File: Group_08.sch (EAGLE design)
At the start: 29 parts, among them J1 POWER_JACKPTH_LOCK, U1 +12v, U3 TCA9546ATSSOP, U4 TMUX1208

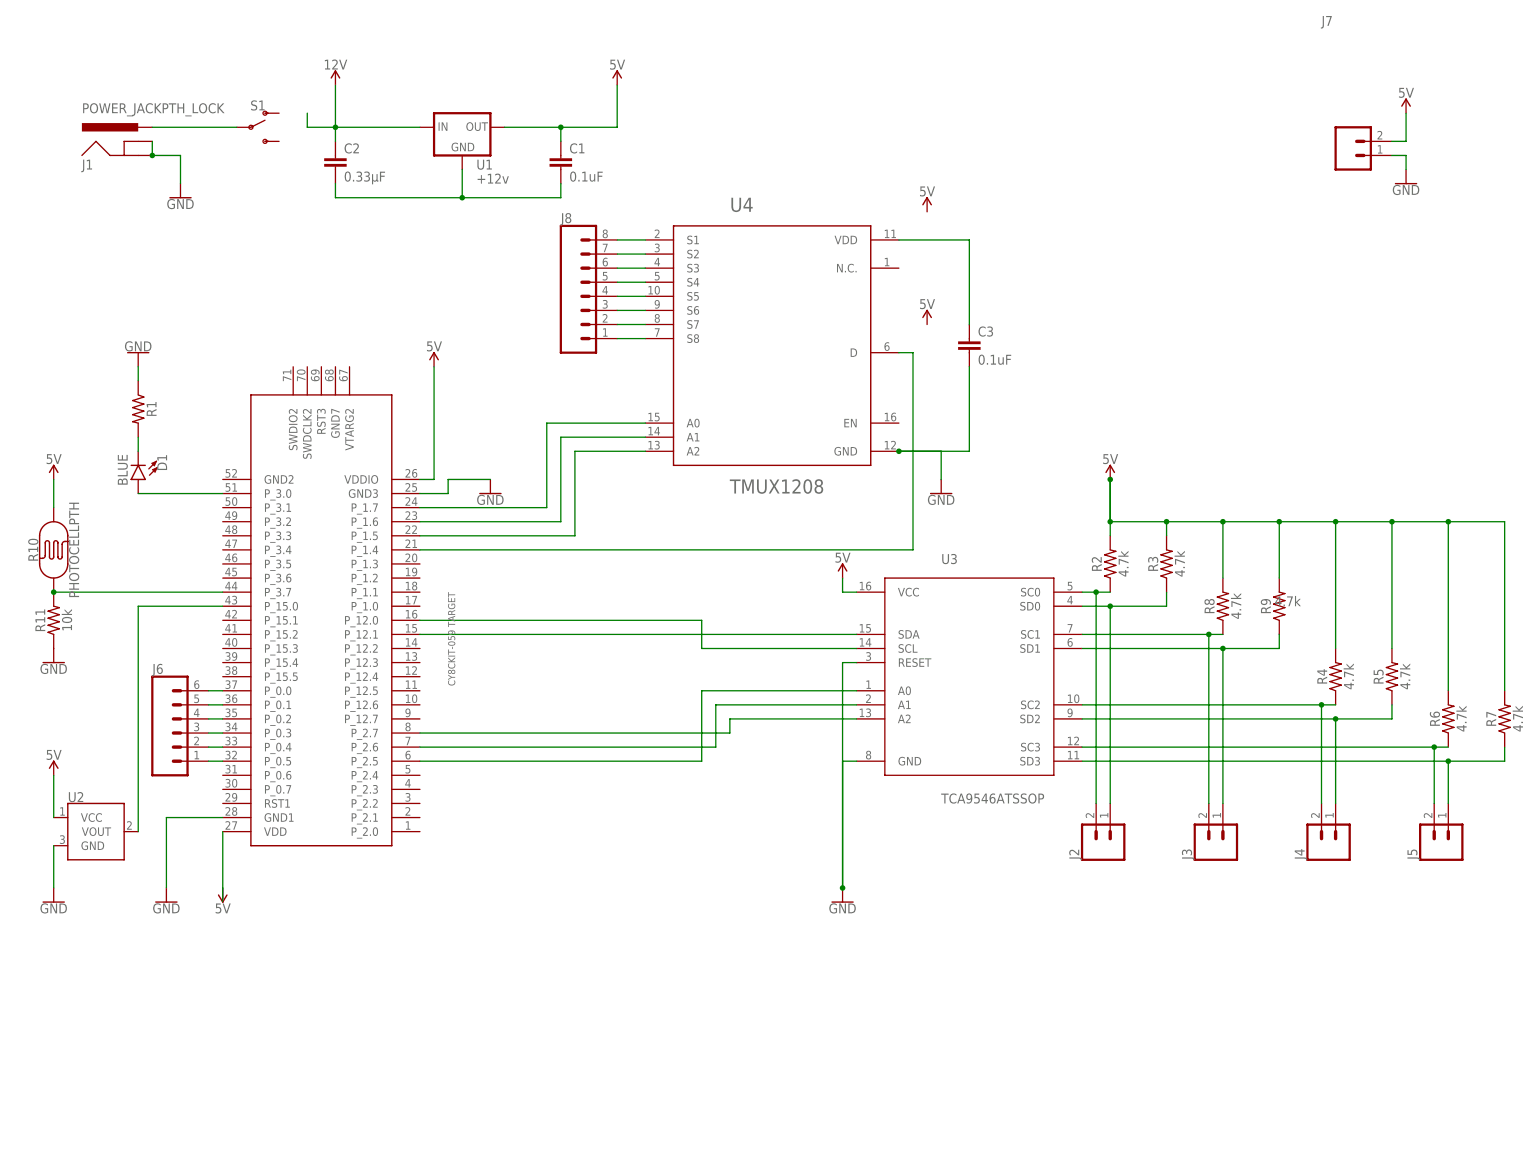
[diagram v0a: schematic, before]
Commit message: Fixed wiring and did small aesthetic adjustments to library symbols
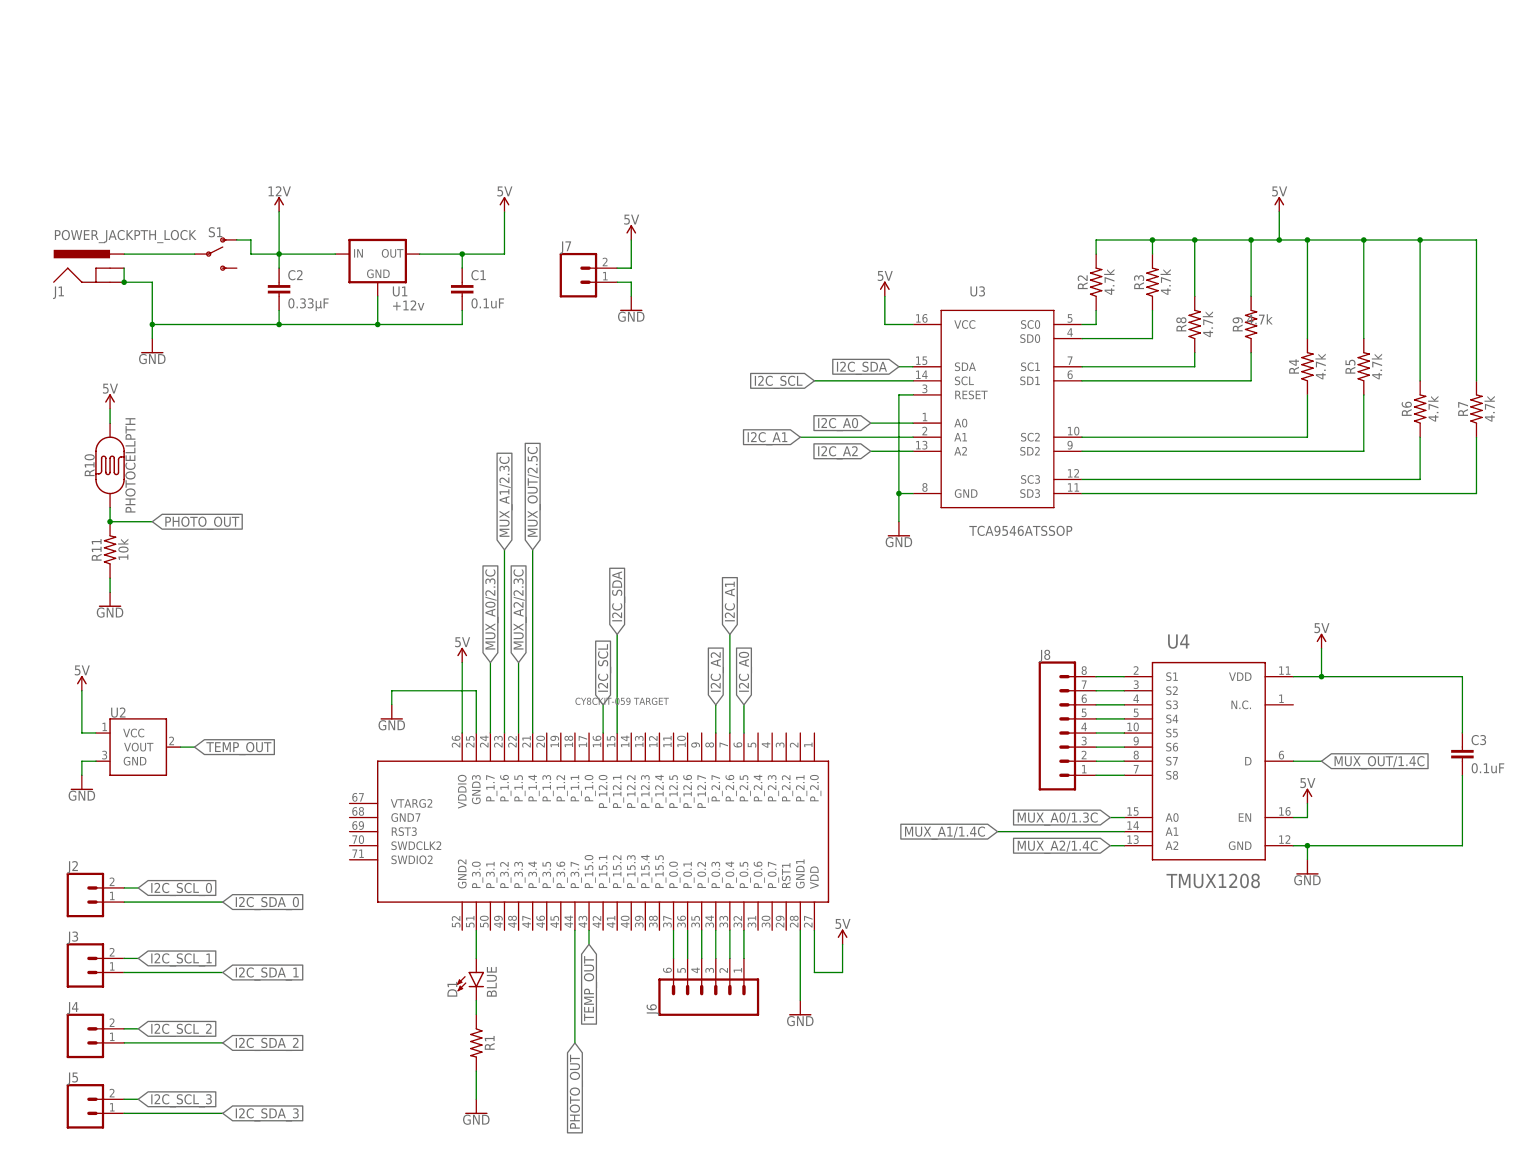
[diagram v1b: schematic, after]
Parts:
- removed U$1: CY8CKIT-059_TARGET, CY8KIT-059:CY8CKIT-059_TARGET
- added CY8CKIT059-TARGET: CY8CKIT-059_TARGET, CY8KIT-059:CY8CKIT-059_TARGET
- R1: value (none) -> RESISTORAXIAL-0.3
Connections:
- removed net N$10 (its old number): U$1.P_2.5, U3.A0
- removed net N$11 (its old number): U$1.P_2.6, U3.A1
- removed net N$12 (its old number): U$1.P_2.7, U3.A2
- removed net N$13 (its old number): U$1.P_12.0, U3.SCL
- removed net N$14 (its old number): U$1.P_12.1, U3.SDA
- removed net N$15: C1.2, C2.2, U1.GND
- removed net N$16 (its old number): J6.6, U$1.P_0.0
- removed net N$17 (its old number): J6.5, U$1.P_0.1
- removed net N$18 (its old number): J6.4, U$1.P_0.2
- removed net N$27: U$1.P_15.0, U2.VOUT
- removed net N$28: D1.C, R1.2
- removed net N$37: C3.1, U4.VDD
- removed net N$38: D1.A, U$1.P_3.0
- new net I2C_A0: CY8CKIT059-TARGET.P_2.5, U3.A0
- new net I2C_A1: CY8CKIT059-TARGET.P_2.6, U3.A1
- new net I2C_A2: CY8CKIT059-TARGET.P_2.7, U3.A2
- new net I2C_SCL: CY8CKIT059-TARGET.P_12.0, U3.SCL
- new net I2C_SCL_0: J2.2
- new net I2C_SCL_1: J3.2
- new net I2C_SCL_2: J4.2
- new net I2C_SCL_3: J5.2
- new net I2C_SDA: CY8CKIT059-TARGET.P_12.1, U3.SDA
- new net I2C_SDA_0: J2.1
- new net I2C_SDA_1: J3.1
- new net I2C_SDA_2: J4.1
- new net I2C_SDA_3: J5.1
- new net MUX_A0/1.3C: U4.A0
- new net MUX_A0/2.3C: CY8CKIT059-TARGET.P_1.7
- new net MUX_A1/1.4C: U4.A1
- new net MUX_A1/2.3C: CY8CKIT059-TARGET.P_1.6
- new net MUX_A2/1.4C: U4.A2
- new net MUX_A2/2.3C: CY8CKIT059-TARGET.P_1.5
- new net MUX_OUT/1.4C: U4.D
- new net MUX_OUT/2.5C: CY8CKIT059-TARGET.P_1.4
- new net PHOTO_OUT: CY8CKIT059-TARGET.P_3.7, R10.P$1, R11.2
- new net TEMP_OUT: CY8CKIT059-TARGET.P_15.0, U2.VOUT
- net 12V: now also S1.O
- net 5V: now also C3.1, CY8CKIT059-TARGET.VDD, CY8CKIT059-TARGET.VDDIO, U4.EN, U4.VDD; no longer U$1.VDD, U$1.VDDIO
- net GND: now also C1.2, C2.2, CY8CKIT059-TARGET.GND1, CY8CKIT059-TARGET.GND3, R1.2, U1.GND; no longer R1.1, U$1.GND1, U$1.GND3
- net N$1: no longer J2.2
- net N$19: now also CY8CKIT059-TARGET.P_0.0, J6.6; no longer J6.3, U$1.P_0.3
- net N$20: now also CY8CKIT059-TARGET.P_0.5, J6.1; no longer J6.2, U$1.P_0.4
- net N$21: now also CY8CKIT059-TARGET.P_0.4, J6.2; no longer J6.1, U$1.P_0.5
- net N$22: now also CY8CKIT059-TARGET.P_0.3, J6.3; no longer U$1.P_1.7, U4.A0
- net N$23: now also CY8CKIT059-TARGET.P_0.2, J6.4; no longer U$1.P_1.6, U4.A1
- net N$24: now also CY8CKIT059-TARGET.P_0.1, J6.5; no longer U$1.P_1.5, U4.A2
- net N$25: now also D1.C, R1.1; no longer U$1.P_1.4, U4.D
- net N$26: now also CY8CKIT059-TARGET.P_3.0, D1.A; no longer R10.P$1, R11.2, U$1.P_3.7
- net N$3: no longer J2.1
- net N$4: no longer J3.2
- net N$5: no longer J3.1
- net N$6: no longer J4.2
- net N$7: no longer J4.1
- net N$8: no longer J5.2
- net N$9: no longer J5.1
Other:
- moved on the sheet: C1, C2, C3, D1, J1, J2, J3, J4, J5, J6, J7, J8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

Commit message: board with almoost all wiring done
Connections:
- net N$3 renamed IDC_SDA_0
- removed net N$1: R2.1, U3.SC0
- removed net N$4: R8.1, U3.SC1
- removed net N$5: R9.1, U3.SD1
- removed net N$6: R4.1, U3.SC2
- removed net N$7: R5.1, U3.SD2
- removed net N$8: R6.1, U3.SC3
- removed net N$9: R7.1, U3.SD3
- net I2C_SCL_0: now also R2.1, U3.SC0
- net I2C_SCL_1: now also R8.1, U3.SC1
- net I2C_SCL_2: now also R4.1, U3.SC2
- net I2C_SCL_3: now also R6.1, U3.SC3
- net I2C_SDA_1: now also R9.1, U3.SD1
- net I2C_SDA_2: now also R5.1, U3.SD2
- net I2C_SDA_3: now also R7.1, U3.SD3

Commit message: Deleted original prototypes and updated file names
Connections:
- removed net IDC_SDA_0: R3.1, U3.SD0
- net I2C_SDA_0: now also R3.1, U3.SD0
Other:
- note added: "4-Channel I2C"
- note added: "Analog Temperature Sensor"
- note added: "I2C Connectors"
- note added: "Light Sensor"
- note added: "Power"

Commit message: Updated schematics connections
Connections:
- removed net MUX_A0/1.3C: U4.A0
- removed net MUX_A0/2.3C: CY8CKIT059-TARGET.P_1.7
- removed net MUX_A1/1.4C: U4.A1
- removed net MUX_A1/2.3C: CY8CKIT059-TARGET.P_1.6
- removed net MUX_A2/1.4C: U4.A2
- removed net MUX_A2/2.3C: CY8CKIT059-TARGET.P_1.5
- removed net MUX_OUT/1.4C: U4.D
- removed net MUX_OUT/2.5C: CY8CKIT059-TARGET.P_1.4
- new net MUX_A0: CY8CKIT059-TARGET.P_1.7, U4.A0
- new net MUX_A1: CY8CKIT059-TARGET.P_1.6, U4.A1
- new net MUX_A2: CY8CKIT059-TARGET.P_1.5, U4.A2
- new net MUX_OUT: CY8CKIT059-TARGET.P_1.4, U4.D
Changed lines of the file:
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@@
-</segment>
-</net>
-<net name="MUX_A0/1.3C" class="0">
-<segment>
-<pinref part="U4" gate="G$1" pin="A0"/>
-<wire x1="200.66" y1="60.96" x2="198.12" y2="60.96" width="0.1524" layer="91"/>
-<label x="198.12" y="60.96" size="1.778" layer="95" rot="R180" xref="yes"/>
-</segment>
-</net>
-<net name="MUX_A1/1.4C" class="0">
-<segment>
-<pinref part="U4" gate="G$1" pin="A1"/>
-<wire x1="200.66" y1="58.42" x2="177.8" y2="58.42" width="0.1524" layer="91"/>
-<label x="177.8" y="58.42" size="1.778" layer="95" rot="R180" xref="yes"/>
-</segment>
-</net>
-<net name="MUX_A2/1.4C" class="0">
-<segment>
-<pinref part="U4" gate="G$1" pin="A2"/>
-<wire x1="200.66" y1="55.88" x2="198.12" y2="55.88" width="0.1524" layer="91"/>
-<label x="198.12" y="55.88" size="1.778" layer="95" rot="R180" xref="yes"/>
-</segment>
-</net>
-<net name="MUX_OUT/1.4C" class="0">
-<segment>
-<pinref part="U4" gate="G$1" pin="D"/>
-<wire x1="231.14" y1="71.12" x2="236.22" y2="71.12" width="0.1524" layer="91"/>
-<label x="236.22" y="71.12" size="1.778" layer="95" xref="yes"/>
 </segment>
 </net>
@@
 </segment>
 </net>
-<net name="MUX_A0/2.3C" class="0">
+<net name="MUX_A0" class="0">
 <segment>
 <pinref part="CY8CKIT059-TARGET" gate="G$1" pin="P_1.7"/>
@@
 <label x="88.9" y="83.82" size="1.778" layer="95" rot="R90" xref="yes"/>
 </segment>
+<segment>
+<pinref part="U4" gate="G$1" pin="A0"/>
+<wire x1="200.66" y1="60.96" x2="198.12" y2="60.96" width="0.1524" layer="91"/>
+<label x="198.12" y="60.96" size="1.778" layer="95" rot="R180" xref="yes"/>
+</segment>
 </net>
-<net name="MUX_A1/2.3C" class="0">
+<net name="MUX_A1" class="0">
 <segment>
 <pinref part="CY8CKIT059-TARGET" gate="G$1" pin="P_1.6"/>
-<wire x1="91.44" y1="78.74" x2="91.44" y2="106.68" width="0.1524" layer="91"/>
-<label x="91.44" y="106.68" size="1.778" layer="95" rot="R90" xref="yes"/>
+<wire x1="91.44" y1="78.74" x2="91.44" y2="101.6" width="0.1524" layer="91"/>
+<label x="91.44" y="101.6" size="1.778" layer="95" rot="R90" xref="yes"/>
+</segment>
+<segment>
+<pinref part="U4" gate="G$1" pin="A1"/>
+<wire x1="200.66" y1="58.42" x2="185.42" y2="58.42" width="0.1524" layer="91"/>
+<label x="185.42" y="58.42" size="1.778" layer="95" rot="R180" xref="yes"/>
 </segment>
 </net>
-<net name="MUX_A2/2.3C" class="0">
+<net name="MUX_A2" class="0">
 <segment>
 <pinref part="CY8CKIT059-TARGET" gate="G$1" pin="P_1.5"/>
@@
 <label x="93.98" y="83.82" size="1.778" layer="95" rot="R90" xref="yes"/>
 </segment>
+<segment>
+<pinref part="U4" gate="G$1" pin="A2"/>
+<wire x1="200.66" y1="55.88" x2="198.12" y2="55.88" width="0.1524" layer="91"/>
+<label x="198.12" y="55.88" size="1.778" layer="95" rot="R180" xref="yes"/>
+</segment>
 </net>
-<net name="MUX_OUT/2.5C" class="0">
+<net name="MUX_OUT" class="0">
 <segment>
 <pinref part="CY8CKIT059-TARGET" gate="G$1" pin="P_1.4"/>
-<wire x1="96.52" y1="78.74" x2="96.52" y2="104.14" width="0.1524" layer="91"/>
-<label x="96.52" y="104.14" size="1.778" layer="95" rot="R90" xref="yes"/>
+<wire x1="96.52" y1="78.74" x2="96.52" y2="101.6" width="0.1524" layer="91"/>
+<label x="96.52" y="101.6" size="1.778" layer="95" rot="R90" xref="yes"/>
+</segment>
+<segment>
+<pinref part="U4" gate="G$1" pin="D"/>
+<wire x1="231.14" y1="71.12" x2="236.22" y2="71.12" width="0.1524" layer="91"/>
+<label x="236.22" y="71.12" size="1.778" layer="95" xref="yes"/>
 </segment>
 </net>
